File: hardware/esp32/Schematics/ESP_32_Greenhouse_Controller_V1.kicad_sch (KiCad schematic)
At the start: 20 parts, among them Q1 DMP1045UQ, Q2 S8050, Q3 2N2222A, Q4 2N2222A, T1 24 V 1 A <-- 230 V, U2 12 V OUT <-- 24 V IN, U3 3.3 V OUT <-- 24 V IN, U6 DHT11

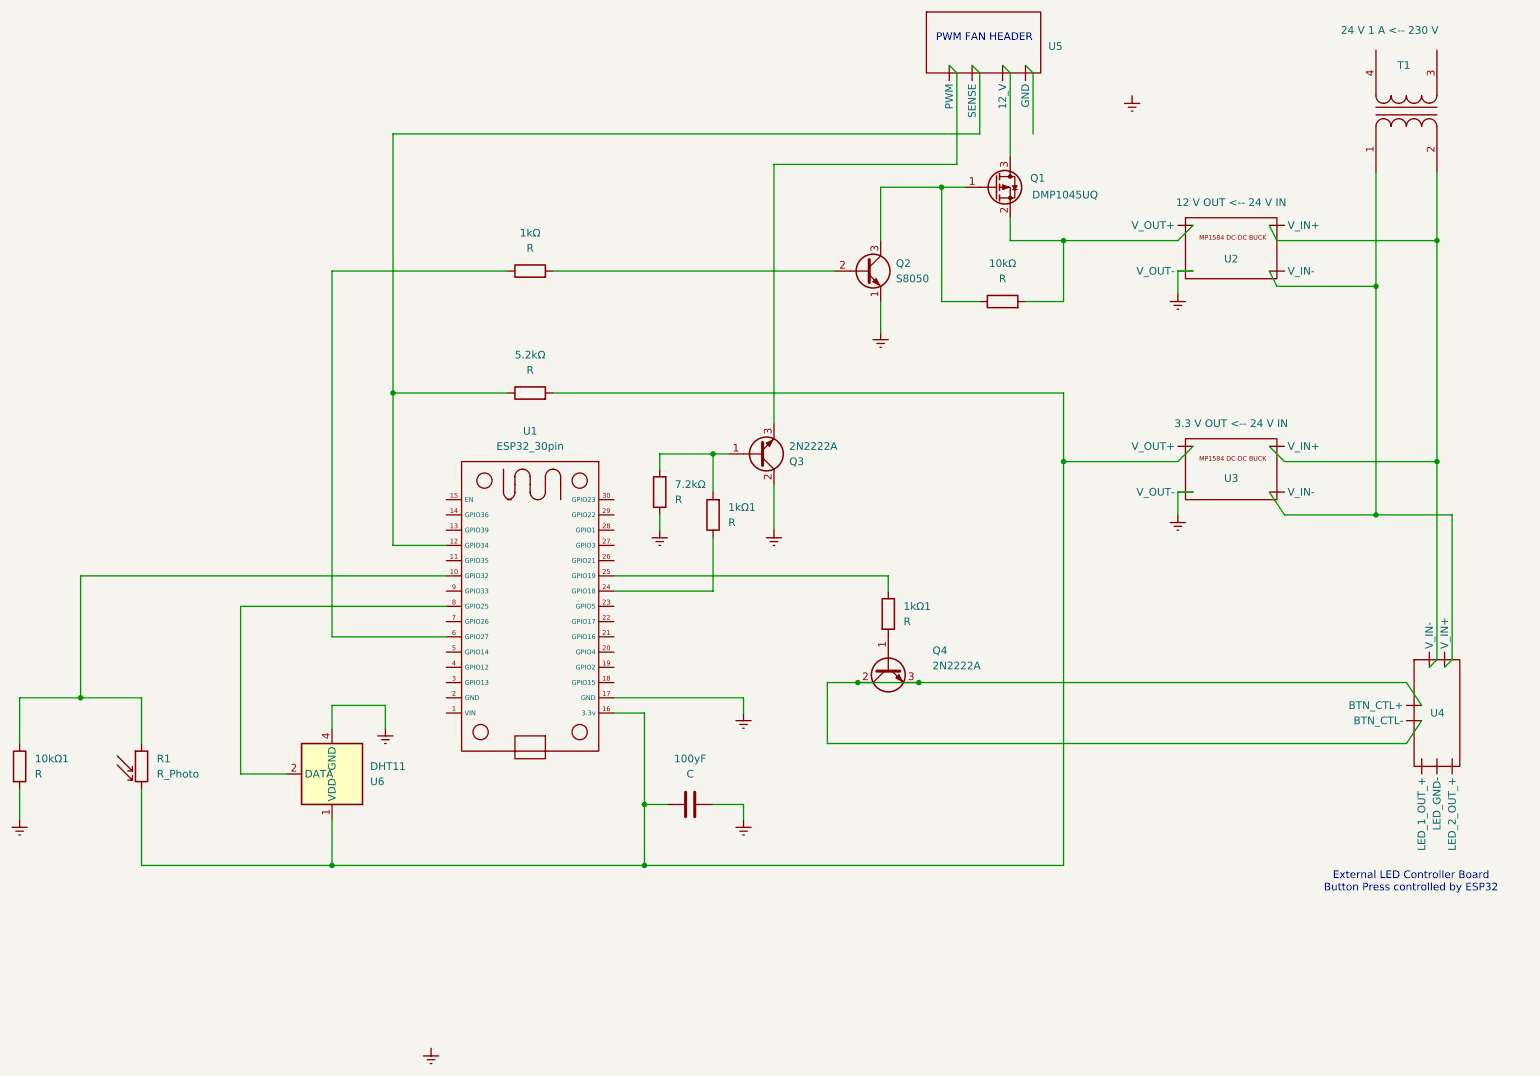
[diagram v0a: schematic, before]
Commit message: Updated Schematic to include pwm controlled LED
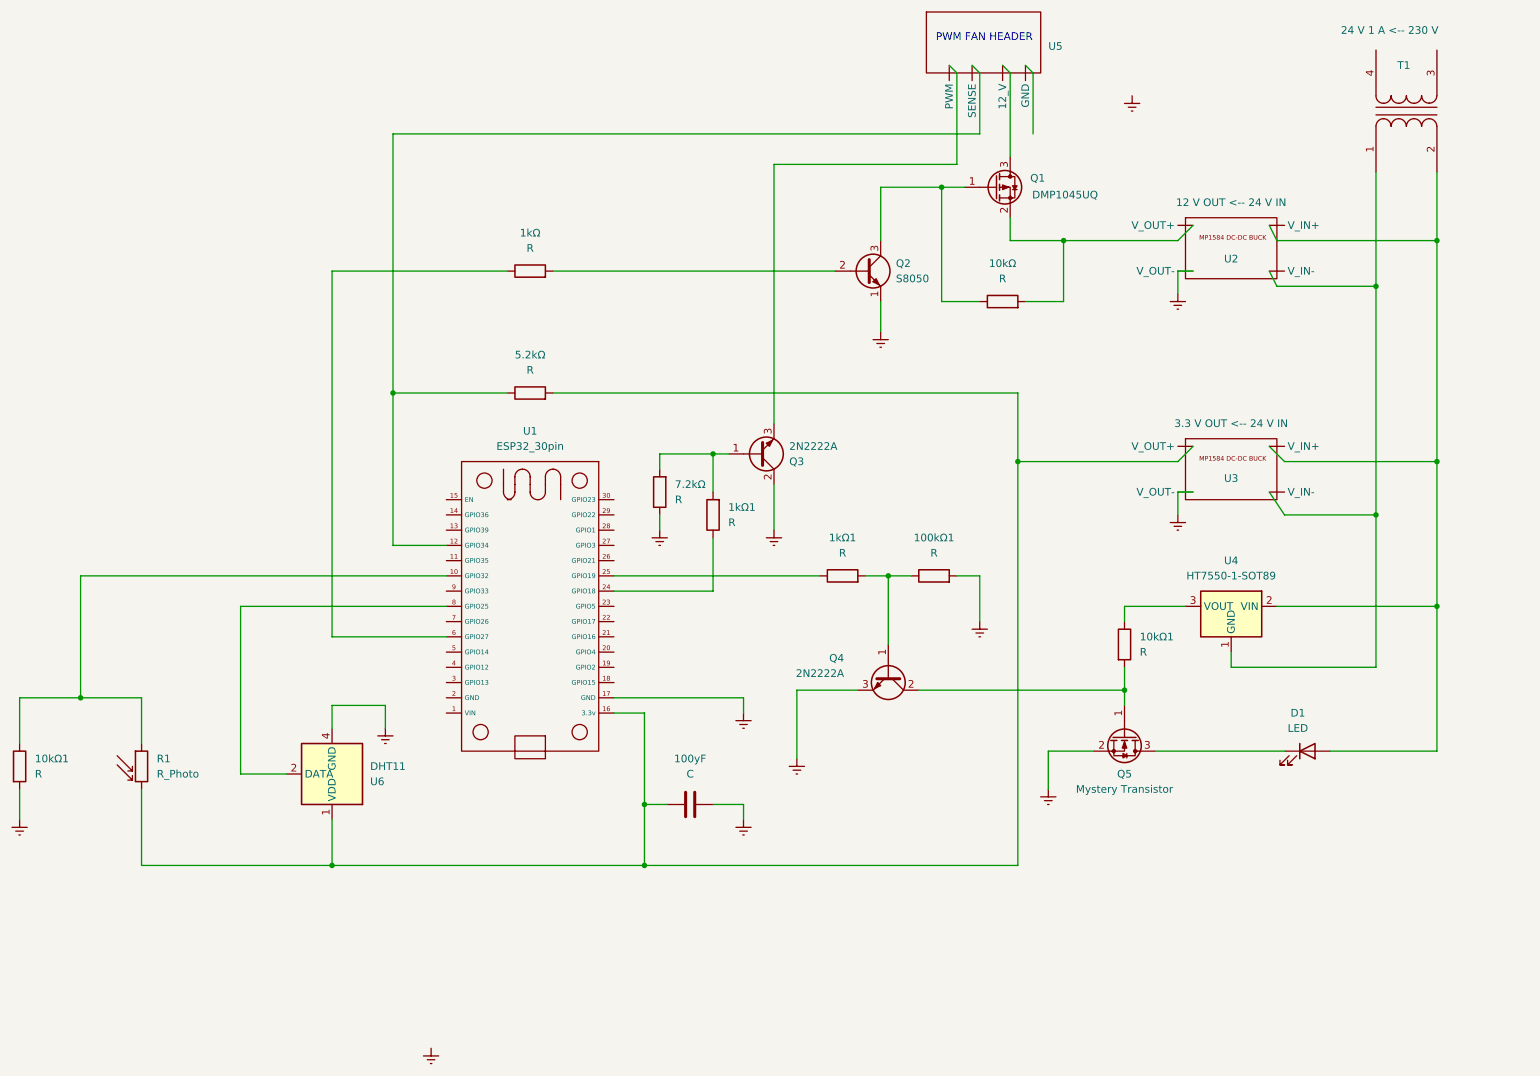
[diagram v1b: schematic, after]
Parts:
- removed U4: (no value), symbol MyModules:LED_CONTROL_PANEL
- added 100kΩ1, 10kΩ1: R, symbol Device:R
- added D1: LED, symbol Device:LED
- added Q5: Mystery Transistor, Package_TO_SOT_SMD:SOT-23, symbol Transistor_FET:2N7002
- added U4: HT7550-1-SOT89, Package_TO_SOT_SMD:SOT-89-3, symbol Regulator_Linear:HT75xx-1-SOT89
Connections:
- net at U3. (V_IN-): now also T1.1 (AA), U2. (V_IN-), U4.1 (GND)
- net at 1kΩ1.2, Q4.1 (B): now also 100kΩ1.1
- net at Q4.2 (C): now also 10kΩ1.2, Q5.1 (G); no longer Q4.3 (E)
- net at U5. (GND): now also Q1.3 (D)
- new net: D1.2 (A), T1.2 (AB), U2. (V_IN-), U3. (V_IN-), U4.2 (VIN)
- new net: D1.1 (K), Q5.3 (D)
- new net: 10kΩ1.1, U4.3 (VOUT)
- now unconnected: U2. (V_IN-), U2. (V_IN-)
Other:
- note removed: "External LED Controller Board Button Press controlled by ESP32"
- moved on the sheet: 1kΩ1, Q4

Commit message: Updated PWM LED Script, first agentic rework; updated Schematic.
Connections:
- net at U3. (V_IN-): now also T1.1 (AA), U2. (V_IN-), U4.1 (GND)
- net at U5. (GND): now also Q1.3 (D)
- now unconnected: U2. (V_IN-)
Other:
- moved on the sheet: 10kΩ, 1kΩ, 5.2kΩ, Q2, Q4

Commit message: Try Try again?
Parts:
- added 10kΩ1, 1kΩ11, 4.7kΩ1: R, symbol Device:R
- added Q6: 2N3906, Package_TO_SOT_THT:TO-92_Inline, symbol Transistor_BJT:2N3906
- renumbered 10kΩ1 to 100Ω1
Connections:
- net at U3. (V_IN-): now also T1.1 (AA), U2. (V_IN-), U4.1 (GND)
- net at U4.3 (VOUT): now also 10kΩ1.2, Q6.1 (E); no longer 100Ω1.1
- net at 100Ω1.2, Q5.1 (G): now also 1kΩ11.2; no longer Q4.2 (C)
- net at Q5.2 (S): now also 1kΩ11.1
- net at U1.17 (GND): now also Q4.3 (E)
- net at U5. (GND): now also Q1.3 (D)
- new net: 5.2kΩ.2, R1.2, U3. (V_IN-)
- new net: 10kΩ1.1, 4.7kΩ1.2, Q6.2 (B)
- new net: 100Ω1.1, Q6.3 (C)
- new net: 100yF.1, U1.16 (3.3v)
- new net: 4.7kΩ1.1, Q4.2 (C)
- now unconnected: U2. (V_IN-), U6.1 (VDD)
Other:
- moved on the sheet: 100kΩ1, 100yF, 100Ω1, 10kΩ1, 1kΩ, 1kΩ1, 5.2kΩ, 7.2kΩ, D1, Q2, Q3, Q4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

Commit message: Preliminary tests passed, minor changes to firm- and hardware of the esp controller. V1 Complete
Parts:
- removed 10kΩ: R, symbol Device:R
- removed Q1: DMP1045UQ, Package_TO_SOT_SMD:SOT-23, symbol Transistor_FET:DMP3099L
- removed Q2: S8050, Package_TO_SOT_THT:TO-92_Inline, symbol Transistor_BJT:S8050
- added Q1: STT4P3LLH6, Package_TO_SOT_SMD:SOT-23-6, symbol Greenhouse:STT4P3LLH6
- added Q7: 2N2222A, symbol Transistor_BJT:Q_NPN_BCE
- added R12, R14: 100kΩ, symbol Device:R
- added R13: 1kΩ, symbol Device:R
- C1: renamed from 100yF; value C -> 100yF
- D1: value LED -> 24 V LED module
- PS1: renamed from T1; value 24 V 1 A <-- 230 V -> 24 V DC / 1 A; symbol Device:Transformer_1P_1S -> Greenhouse:External_24V_DC_Source
- Q5: value Mystery Transistor -> Mystery transistor - TBD; footprint Package_TO_SOT_SMD:SOT-23 -> (none); symbol Transistor_FET:2N7002 -> Greenhouse:Unidentified_NMOS
- R10: renamed from 1kΩ; value R -> 10kΩ
- R11: renamed from 5.2kΩ; value R -> 5.2kΩ
- R15: renamed from 1kΩ11; value R -> 10kΩ
- R2: renamed from 100Ω1; value R -> 100Ω
- R3, R7: renamed from 10kΩ1; value R -> 10kΩ
- R4: renamed from 4.7kΩ1; value R -> 4.7kΩ
- R5: renamed from 100kΩ1; value R -> 100kΩ
- R6, R8: renamed from 1kΩ1; value R -> 1kΩ
- R9: renamed from 7.2kΩ; value R -> 7.2kΩ
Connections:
- net GNDREF: now reaches U3. (V_IN-)
- net GNDREF: now also C1.2, PS1.2 (0V), Q3.3 (E), Q4.3 (E), Q5.2 (S), R15.1, R5.2, R7.2, R9.1, U1.17 (GND), U2. (V_IN-), U4.1 (GND), U5.1 (GND), U6.4 (GND), Q7.3 (E), R14.2
- net at R11.1, U1.12 (GPIO34): now also U5.3 (SENSE); no longer U5. (GND)
- net at R10.1, U1.6 (GPIO27): now also R14.1
- net at R10.2: now also Q7.1 (B)
- net at Q3.2 (C): now also U5.4 (PWM)
- new net: D1.2 (A), PS1.1 (+24V), U2. (V_IN-), U3. (V_IN-), U4.2 (VIN)
- new net: Q1.1 (D), Q1.2 (D), Q1.5 (D), Q1.6 (D), U5.2 (12_V)
- new net: Q1.3 (G), R12.1, R13.2
- new net: Q1.4 (S), R12.2, U2. (V_IN-)
- new net: Q7.2 (C), R13.1
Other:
- moved on the sheet: D1, Q3, Q6, R10, R11, R15, R2, R3, R4, R5, R6, R8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

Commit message: Addtion to previous commit
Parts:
- added C2, C3: 10µF, symbol Device:C
- C1: value 100yF -> 100µF
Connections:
- net GNDREF: now also C2.1, C3.2
- net at D1.2 (A), PS1.1 (+24V), U2. (V_IN-)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: now also C2.2
- net at Q6.1 (E), R3.2, U4.3 (VOUT): now also C3.1
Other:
- moved on the sheet: Q5, Q6, R15, R2, R3
